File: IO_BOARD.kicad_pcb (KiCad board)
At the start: 4 copper layers, 18 x 23.5 mm, 6 parts, among them J2 TYPE-C-31-M-12

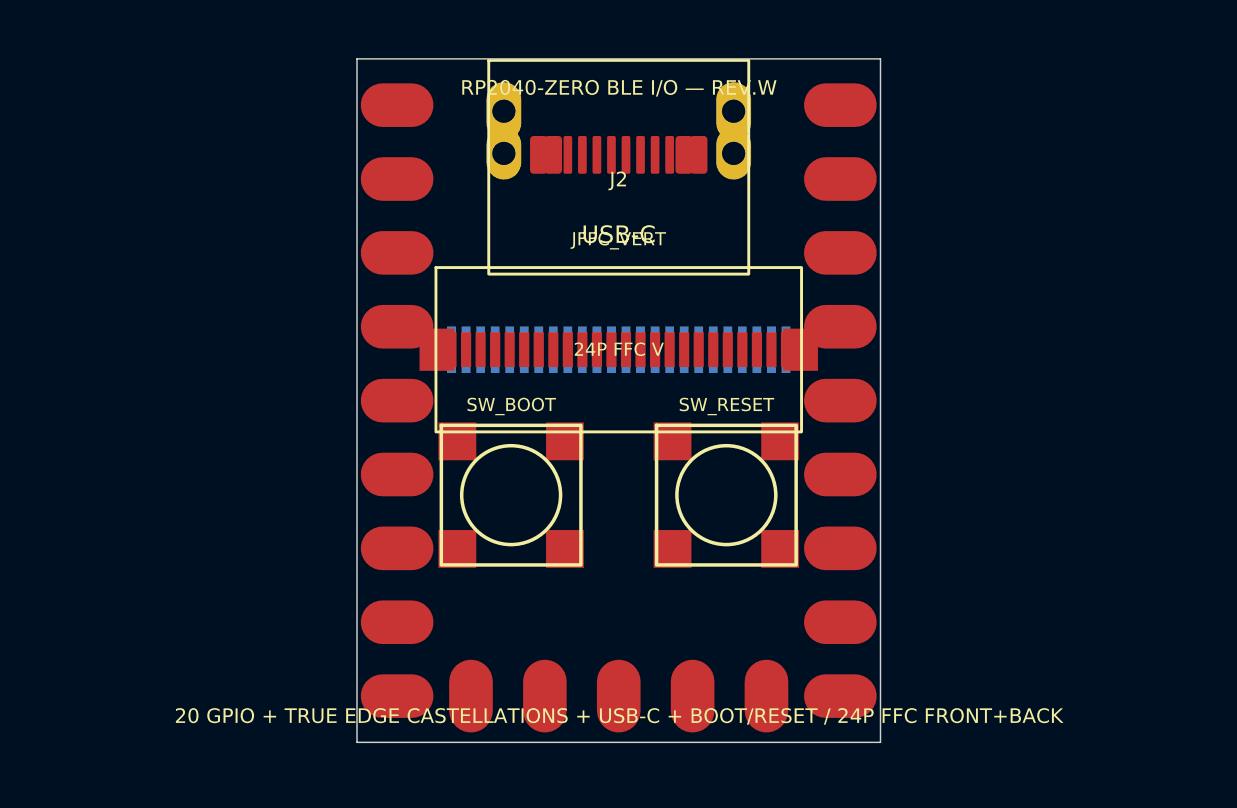
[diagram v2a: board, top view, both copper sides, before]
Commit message: Restore exact RP2040-Zero THT castellated master geometry
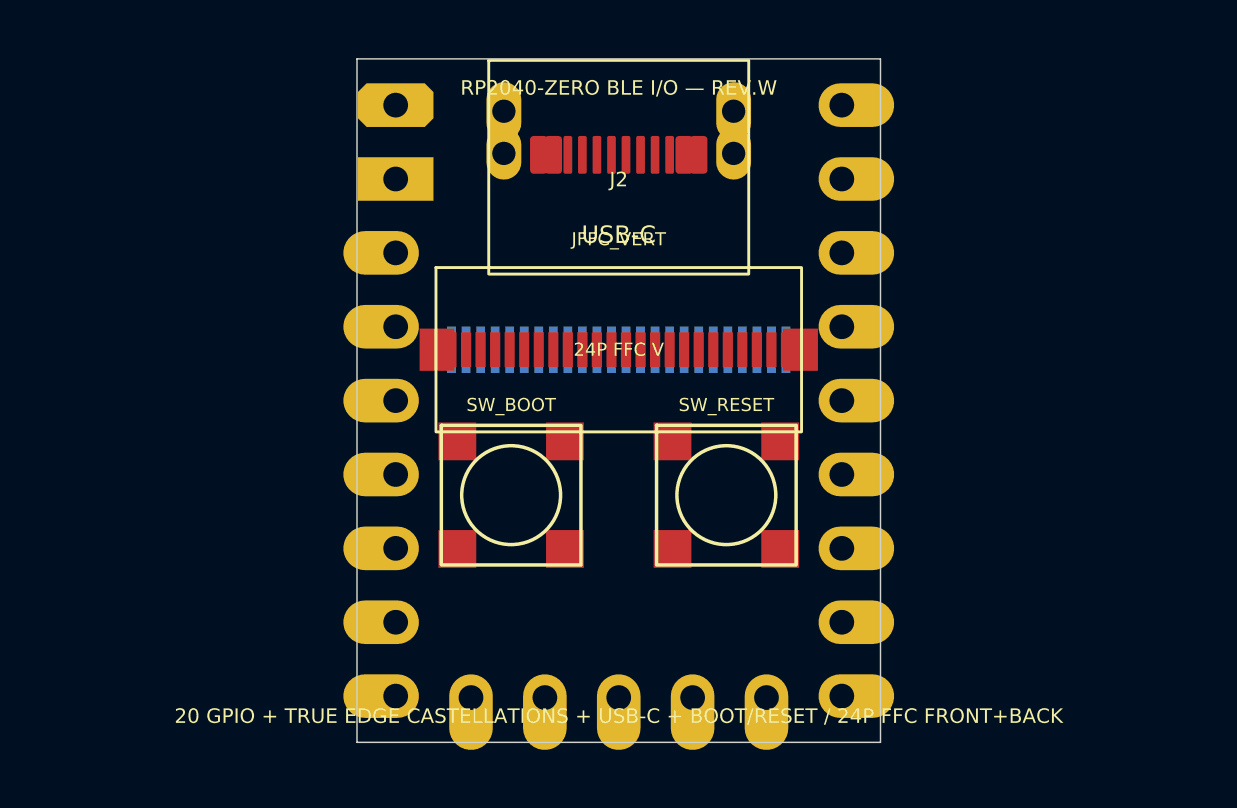
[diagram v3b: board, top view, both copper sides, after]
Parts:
- removed the JLEG at (0.00, 0.00)
- added JLEG: RP2040-Zero-THT, RP2040-Zero-THT-Castellation-Master, F.Cu at (0.00, 0.00)
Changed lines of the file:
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@@
  (gr_text "RP2040-ZERO BLE I/O — REV.W" (at 9 1.0) (layer "F.SilkS") (effects (font (size 0.5 0.5) (thickness 0.1))))
  (gr_text "20 GPIO + TRUE EDGE CASTELLATIONS + USB-C + BOOT/RESET / 24P FFC FRONT+BACK" (at 9 22.6) (layer "F.SilkS") (effects (font (size 0.5 0.5) (thickness 0.1))))
- (footprint "RP2040-Zero-Castellated-Master" (layer "F.Cu") (at 0 0)
-  (fp_text reference "JLEG" (at 9 0.7) (layer "F.SilkS") hide
-    (effects (font (size 0.5 0.5) (thickness 0.08))))
-  (fp_text value "RP2040-Zero castellated mechanical master" (at 9 22.8) (layer "F.Fab") hide
-    (effects (font (size 0.8 0.8) (thickness 0.12))))
-  (pad "0" smd oval (at 16.62 1.59 180) (size 2.50 1.50) (layers "F.Cu" "F.Paste" "F.Mask") (net 1 "GPIO0"))
-  (pad "1" smd oval (at 16.62 4.13 180) (size 2.50 1.50) (layers "F.Cu" "F.Paste" "F.Mask") (net 2 "GPIO1"))
-  (pad "2" smd oval (at 16.62 6.67 180) (size 2.50 1.50) (layers "F.Cu" "F.Paste" "F.Mask") (net 3 "GPIO2"))
-  (pad "3" smd oval (at 16.62 9.21 180) (size 2.50 1.50) (layers "F.Cu" "F.Paste" "F.Mask") (net 4 "GPIO3"))
-  (pad "4" smd oval (at 16.62 11.75 180) (size 2.50 1.50) (layers "F.Cu" "F.Paste" "F.Mask") (net 5 "GPIO4"))
-  (pad "5" smd oval (at 16.62 14.29 180) (size 2.50 1.50) (layers "F.Cu" "F.Paste" "F.Mask") (net 6 "GPIO5"))
-  (pad "6" smd oval (at 16.62 16.83 180) (size 2.50 1.50) (layers "F.Cu" "F.Paste" "F.Mask") (net 7 "GPIO6"))
-  (pad "7" smd oval (at 16.62 19.37 180) (size 2.50 1.50) (layers "F.Cu" "F.Paste" "F.Mask") (net 8 "GPIO7"))
-  (pad "8" smd oval (at 16.62 21.91 180) (size 2.50 1.50) (layers "F.Cu" "F.Paste" "F.Mask") (net 9 "GPIO8"))
-  (pad "9" smd oval (at 14.08 21.91 90) (size 2.50 1.50) (layers "F.Cu" "F.Paste" "F.Mask") (net 10 "GPIO9"))
-  (pad "10" smd oval (at 11.54 21.91 90) (size 2.50 1.50) (layers "F.Cu" "F.Paste" "F.Mask") (net 11 "GPIO10"))
-  (pad "11" smd oval (at 9.00 21.91 90) (size 2.50 1.50) (layers "F.Cu" "F.Paste" "F.Mask") (net 12 "GPIO11"))
-  (pad "12" smd oval (at 6.46 21.91 90) (size 2.50 1.50) (layers "F.Cu" "F.Paste" "F.Mask") (net 13 "GPIO12"))
-  (pad "13" smd oval (at 3.92 21.91 90) (size 2.50 1.50) (layers "F.Cu" "F.Paste" "F.Mask") (net 14 "GPIO13"))
-  (pad "14" smd oval (at 1.38 21.91 0) (size 2.50 1.50) (layers "F.Cu" "F.Paste" "F.Mask") (net 15 "GPIO14"))
-  (pad "15" smd oval (at 1.38 19.37 0) (size 2.50 1.50) (layers "F.Cu" "F.Paste" "F.Mask") (net 16 "GPIO15"))
-  (pad "16" smd oval (at 1.38 16.83 0) (size 2.50 1.50) (layers "F.Cu" "F.Paste" "F.Mask") (net 17 "GPIO26"))
-  (pad "17" smd oval (at 1.38 14.29 0) (size 2.50 1.50) (layers "F.Cu" "F.Paste" "F.Mask") (net 18 "GPIO27"))
-  (pad "18" smd oval (at 1.38 11.75 0) (size 2.50 1.50) (layers "F.Cu" "F.Paste" "F.Mask") (net 19 "GPIO28"))
-  (pad "19" smd oval (at 1.38 9.21 0) (size 2.50 1.50) (layers "F.Cu" "F.Paste" "F.Mask") (net 20 "GPIO29"))
-  (pad "20" smd oval (at 1.38 6.67 0) (size 2.50 1.50) (layers "F.Cu" "F.Paste" "F.Mask") (net 21 "3V3"))
-  (pad "21" smd oval (at 1.38 4.13 0) (size 2.50 1.50) (layers "F.Cu" "F.Paste" "F.Mask") (net 22 "GND"))
-  (pad "22" smd oval (at 1.38 1.59 0) (size 2.50 1.50) (layers "F.Cu" "F.Paste" "F.Mask") (net 23 "VSYS"))
+ (footprint "RP2040-Zero-THT-Castellation-Master" (layer "F.Cu") (at 0 0)
+  (fp_text reference "JLEG" (at 9 0.7) (layer "F.SilkS") hide (effects (font (size 0.5 0.5) (thickness 0.08))))
+  (fp_text value "RP2040-Zero-THT" (at 9 22.8) (layer "F.Fab") hide (effects (font (size 0.8 0.8) (thickness 0.12))))
+  (pad "0" thru_hole oval (at 16.67 1.59 180) (size 2.60 1.50) (drill 0.85 (offset -0.50 0)) (layers "*.Cu" "*.Mask") (remove_unused_layers no) (net 1 "GPIO0"))
+  (pad "1" thru_hole oval (at 16.67 4.13 180) (size 2.60 1.50) (drill 0.85 (offset -0.50 0)) (layers "*.Cu" "*.Mask") (remove_unused_layers no) (net 2 "GPIO1"))
+  (pad "2" thru_hole oval (at 16.67 6.67 180) (size 2.60 1.50) (drill 0.85 (offset -0.50 0)) (layers "*.Cu" "*.Mask") (remove_unused_layers no) (net 3 "GPIO2"))
+  (pad "3" thru_hole oval (at 16.67 9.21 180) (size 2.60 1.50) (drill 0.85 (offset -0.50 0)) (layers "*.Cu" "*.Mask") (remove_unused_layers no) (net 4 "GPIO3"))
+  (pad "4" thru_hole oval (at 16.67 11.75 180) (size 2.60 1.50) (drill 0.85 (offset -0.50 0)) (layers "*.Cu" "*.Mask") (remove_unused_layers no) (net 5 "GPIO4"))
+  (pad "5" thru_hole oval (at 16.67 14.29 180) (size 2.60 1.50) (drill 0.85 (offset -0.50 0)) (layers "*.Cu" "*.Mask") (remove_unused_layers no) (net 6 "GPIO5"))
+  (pad "6" thru_hole oval (at 16.67 16.83 180) (size 2.60 1.50) (drill 0.85 (offset -0.50 0)) (layers "*.Cu" "*.Mask") (remove_unused_layers no) (net 7 "GPIO6"))
+  (pad "7" thru_hole oval (at 16.67 19.37 180) (size 2.60 1.50) (drill 0.85 (offset -0.50 0)) (layers "*.Cu" "*.Mask") (remove_unused_layers no) (net 8 "GPIO7"))
+  (pad "8" thru_hole oval (at 16.67 21.91 180) (size 2.60 1.50) (drill 0.85 (offset -0.50 0)) (layers "*.Cu" "*.Mask") (remove_unused_layers no) (net 9 "GPIO8"))
+  (pad "9" thru_hole oval (at 14.08 21.96 90) (size 2.60 1.50) (drill 0.85 (offset -0.50 0)) (layers "*.Cu" "*.Mask") (remove_unused_layers no) (net 10 "GPIO9"))
+  (pad "10" thru_hole oval (at 11.54 21.96 90) (size 2.60 1.50) (drill 0.85 (offset -0.50 0)) (layers "*.Cu" "*.Mask") (remove_unused_layers no) (net 11 "GPIO10"))
+  (pad "11" thru_hole oval (at 9 21.96 90) (size 2.60 1.50) (drill 0.85 (offset -0.50 0)) (layers "*.Cu" "*.Mask") (remove_unused_layers no) (net 12 "GPIO11"))
+  (pad "12" thru_hole oval (at 6.46 21.96 90) (size 2.60 1.50) (drill 0.85 (offset -0.50 0)) (layers "*.Cu" "*.Mask") (remove_unused_layers no) (net 13 "GPIO12"))
+  (pad "13" thru_hole oval (at 3.92 21.96 90) (size 2.60 1.50) (drill 0.85 (offset -0.50 0)) (layers "*.Cu" "*.Mask") (remove_unused_layers no) (net 14 "GPIO13"))
+  (pad "14" thru_hole oval (at 1.33 21.91 0) (size 2.60 1.50) (drill 0.85 (offset -0.50 0)) (layers "*.Cu" "*.Mask") (remove_unused_layers no) (net 15 "GPIO14"))
+  (pad "15" thru_hole oval (at 1.33 19.37 0) (size 2.60 1.50) (drill 0.85 (offset -0.50 0)) (layers "*.Cu" "*.Mask") (remove_unused_layers no) (net 16 "GPIO15"))
+  (pad "26" thru_hole oval (at 1.33 16.83 0) (size 2.60 1.50) (drill 0.85 (offset -0.50 0)) (layers "*.Cu" "*.Mask") (remove_unused_layers no) (net 17 "GPIO26"))
+  (pad "27" thru_hole oval (at 1.33 14.29 0) (size 2.60 1.50) (drill 0.85 (offset -0.50 0)) (layers "*.Cu" "*.Mask") (remove_unused_layers no) (net 18 "GPIO27"))
+  (pad "28" thru_hole oval (at 1.33 11.75 0) (size 2.60 1.50) (drill 0.85 (offset -0.50 0)) (layers "*.Cu" "*.Mask") (remove_unused_layers no) (net 19 "GPIO28"))
+  (pad "29" thru_hole oval (at 1.33 9.21 0) (size 2.60 1.50) (drill 0.85 (offset -0.50 0)) (layers "*.Cu" "*.Mask") (remove_unused_layers no) (net 20 "GPIO29"))
+  (pad "30" thru_hole oval (at 1.33 6.67 0) (size 2.60 1.50) (drill 0.85 (offset -0.50 0)) (layers "*.Cu" "*.Mask") (remove_unused_layers no) (net 21 "3V3"))
+  (pad "31" thru_hole rect (at 1.33 4.13 0) (size 2.60 1.50) (drill 0.85) (layers "*.Cu" "*.Mask") (remove_unused_layers no) (net 22 "GND"))
+  (pad "32" thru_hole roundrect (at 1.33 1.59 0) (size 2.60 1.50) (drill 0.85) (layers "*.Cu" "*.Mask") (remove_unused_layers no) (roundrect_rratio 0) (chamfer_ratio 0.2) (chamfer top_left top_right bottom_left bottom_right) (net 23 "VSYS"))
  )
 (footprint "TYPE-C-31-M-12" (layer "F.Cu") (at 9.0 0.25)
